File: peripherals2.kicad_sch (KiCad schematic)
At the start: 10 parts, among them J4 MSD-4-A, U8 GSDA213, U9 VEML3235SL

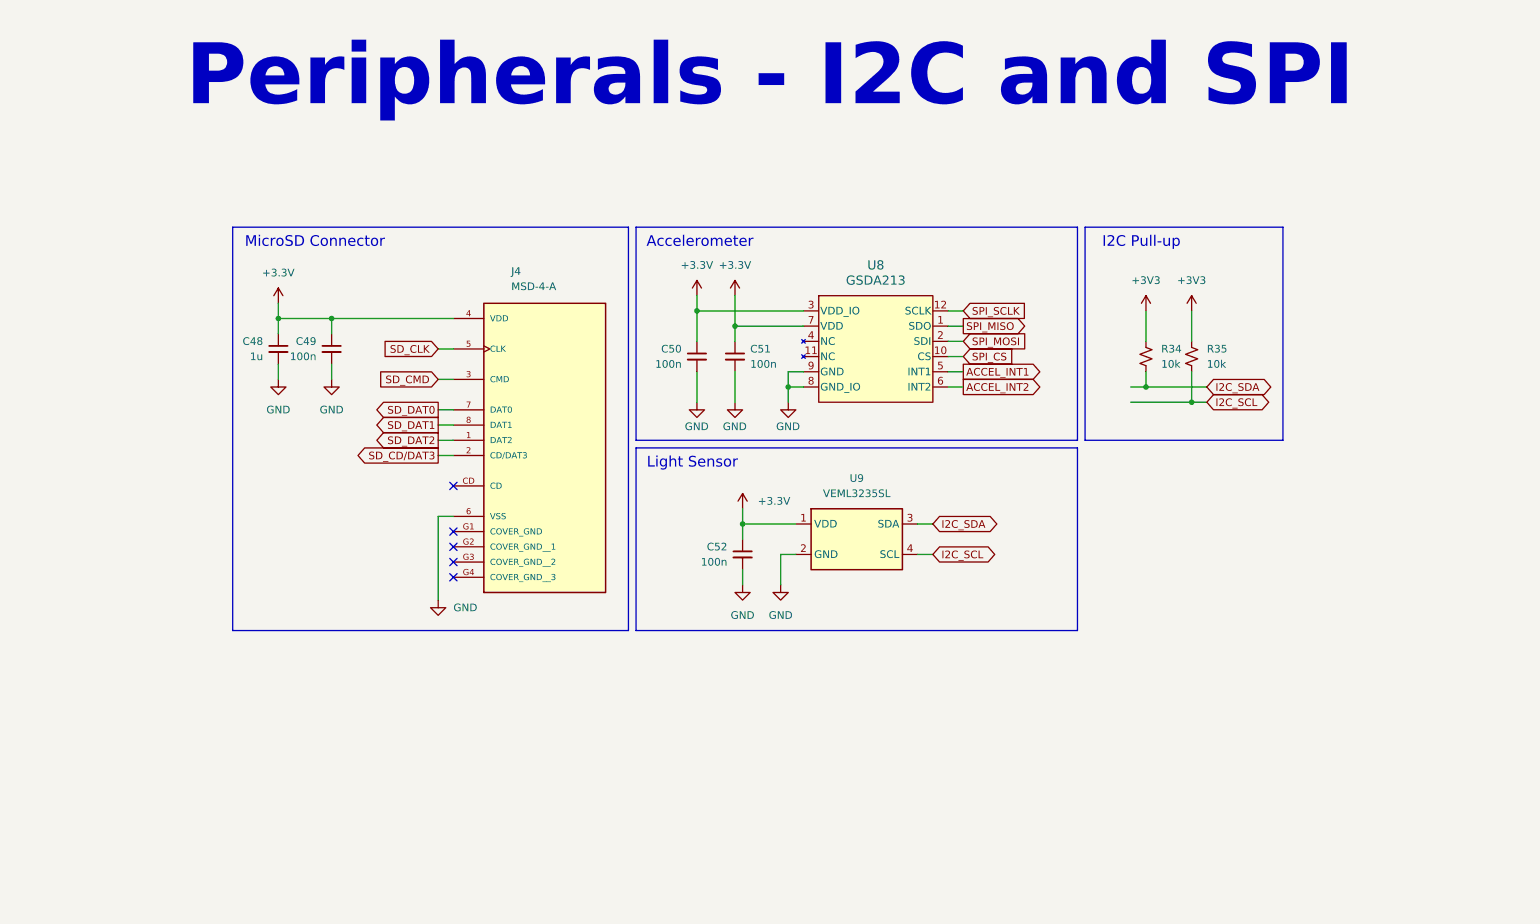
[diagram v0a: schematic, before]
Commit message: feat: adds display circuit
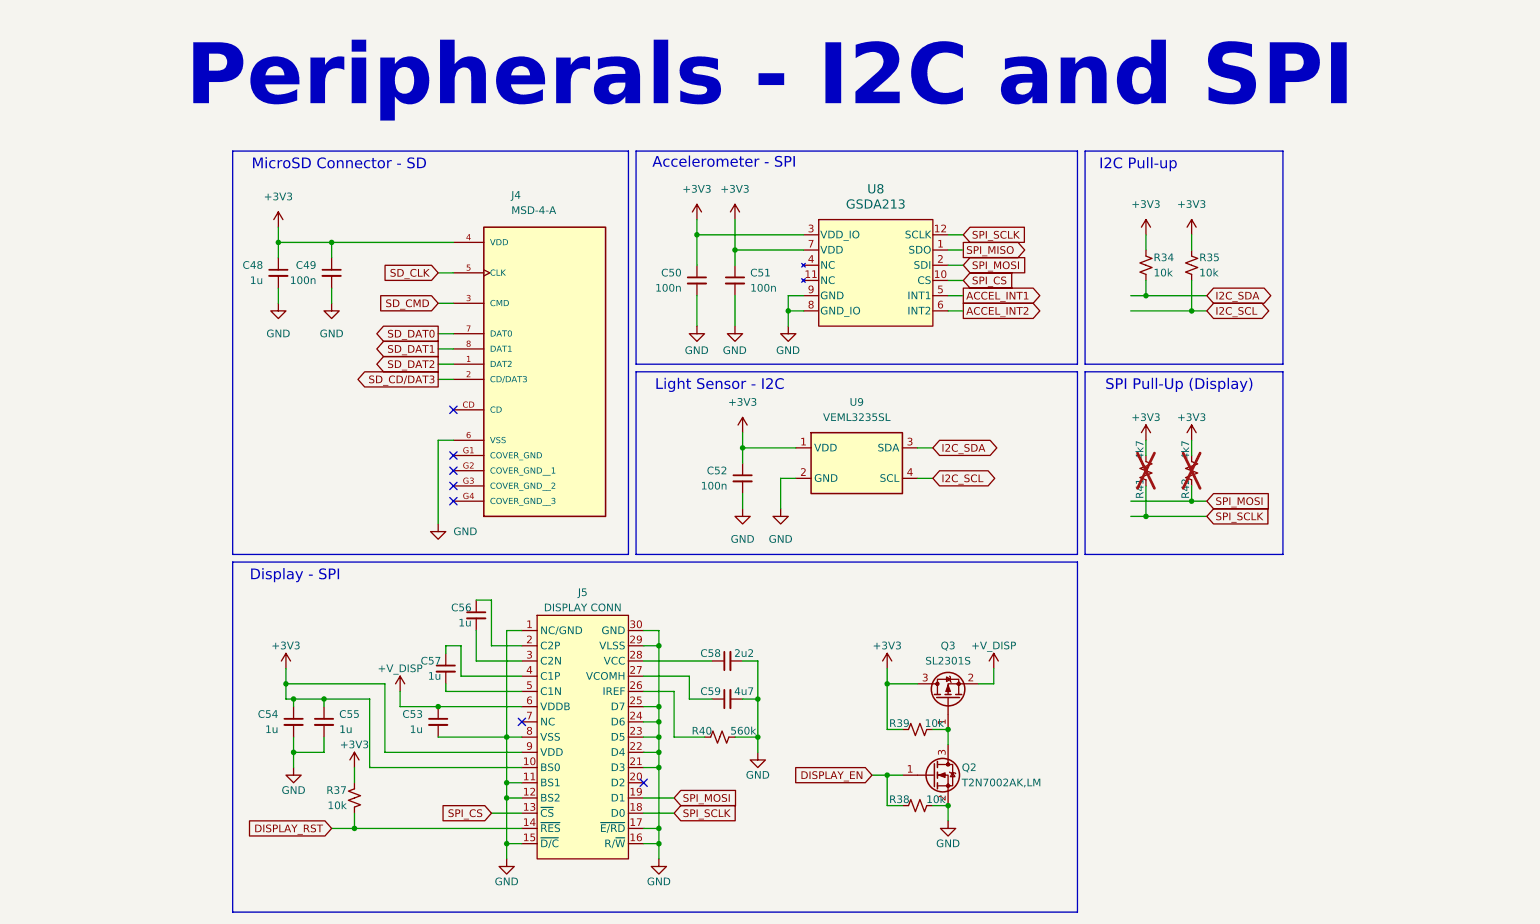
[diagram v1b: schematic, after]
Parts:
- added C53, C54, C55, C56, C57: 1u, Capacitor_SMD:C_0402_1005Metric, symbol Device:C_Small
- added C58: 2u2, Capacitor_SMD:C_0603_1608Metric, symbol Device:C_Small
- added C59: 4u7, Capacitor_SMD:C_0402_1005Metric, symbol Device:C_Small
- added J5: DISPLAY CONN, peripherals2:FPC_30, symbol peripherals2:DISPLAY_CONN
- added Q2: T2N7002AK,LM, Package_TO_SOT_SMD:SOT-23, symbol Transistor_FET:T2N7002AK
- added Q3: SL2301S, Package_TO_SOT_SMD:SOT-23, symbol Transistor_FET:AO3401A
- added R37, R38, R39: 10k, Resistor_SMD:R_0402_1005Metric, symbol Device:R_Small_US
- added R40: 560k, Resistor_SMD:R_0402_1005Metric, symbol Device:R_Small_US
- added R41, R42: 4k7, Resistor_SMD:R_0402_1005Metric, symbol Device:R_Small_US
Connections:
- net +3.3V is gone; now on net +3V3: C48.1, C49.1, C50.1, C51.1, C52.1, J4.4 (VDD), U8.3 (VDD_IO), U8.7 (VDD), U9.1 (VDD)
- net +3V3: now also C54.1, C55.1, J5.10 (BS0), J5.9 (VDD), Q3.3 (D), R37.1, R39.1, R41.2, R42.2
- net GND: now also C53.2, C54.2, C55.2, C58.2, C59.2, J5.1 (NC/GND), J5.11 (BS1), J5.12 (BS2), J5.15 (~{D/C}), J5.16 (R/~{W}), J5.17 (~{E/RD}), J5.21 (D3), J5.22 (D4), J5.23 (D5), J5.24 (D6), J5.25 (D7), J5.29 (VLSS), J5.30 (GND), J5.8 (VSS), Q2.2 (S), R38.2, R40.2
- net SPI_CS: now also J5.13 (~{CS})
- net SPI_MOSI: now also J5.19 (D1), R42.1
- net SPI_SCLK: now also J5.18 (D0), R41.1
- new net: C57.1, J5.4 (C1P)
- new net: C57.2, J5.5 (C1N)
- new net: C58.1, J5.28 (VCC)
- new net: Q2.3 (D), Q3.1 (G), R39.2
- new net: C56.1, J5.2 (C2P)
- new net: C56.2, J5.3 (C2N)
- new net: C59.1, J5.27 (VCOMH)
- new net: J5.26 (IREF), R40.1
- new net +V_DISP: C53.1, J5.6 (VDDB), Q3.2 (S)
- new net DISPLAY_EN: Q2.1 (G), R38.1
- new net DISPLAY_RST: J5.14 (~{RES}), R37.2
- no-connect marks 5 -> 7
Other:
- note added: "Accelerometer - SPI"
- note added: "Display - SPI"
- note added: "Light Sensor - I2C"
- note added: "MicroSD Connector - SD"
- note added: "SPI Pull-Up (Display)"
- note removed: "Accelerometer"
- note removed: "Light Sensor"
- note removed: "MicroSD Connector"
- moved on the sheet: C48, C49, C50, C51, C52, J4, R34, R35, U8, U9

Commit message: feat: connects SPI and I2C pins to MCU
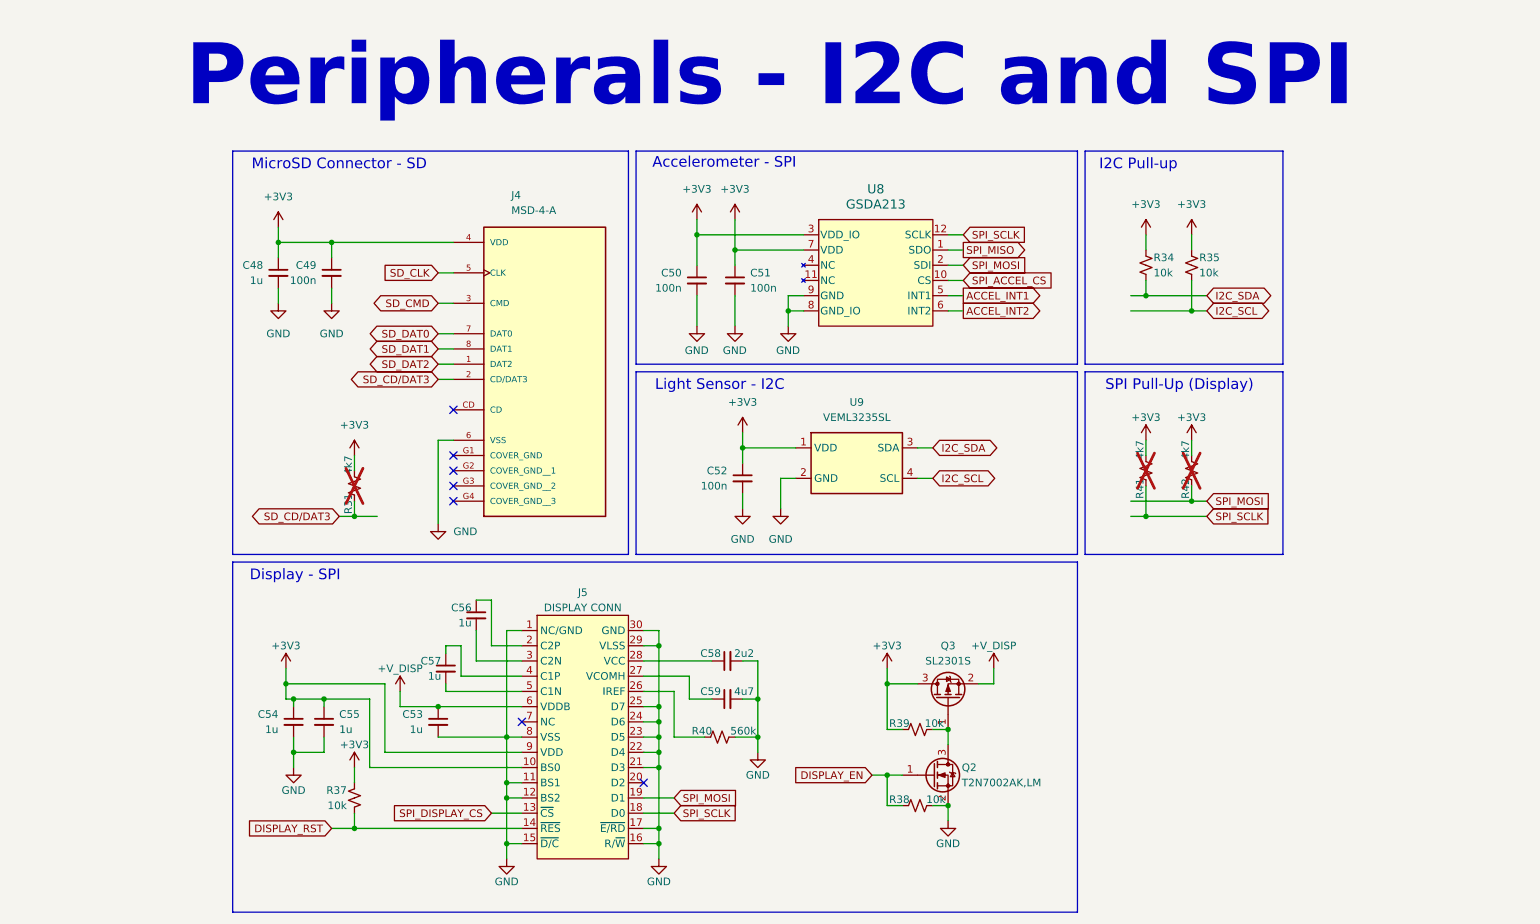
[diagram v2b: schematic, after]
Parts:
- added R31: 4k7, Resistor_SMD:R_0402_1005Metric, symbol Device:R_Small_US
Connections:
- net +3V3: now also R31.2
- net SD_CD/DAT3: now also R31.1
- net SPI_CS renamed SPI_ACCEL_CS
- net SPI_ACCEL_CS: no longer J5.13 (~{CS})
- new net SPI_DISPLAY_CS: J5.13 (~{CS})
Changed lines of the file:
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@@
 	)
 	(junction
+		(at 82.55 97.79)
+		(diameter 0)
+		(color 0 0 0 0)
+	)
+	(junction
 		(at 78.74 52.07)
 		(diameter 0)
@@
 	(wire
 		(pts
+			(xy 82.55 87.63) (xy 82.55 90.17)
+		)
+		(stroke
+			(width 0)
+			(type default)
+		)
+	)
+	(wire
+		(pts
+			(xy 82.55 97.79) (xy 86.36 97.79)
+		)
+		(stroke
+			(width 0)
+			(type default)
+		)
+	)
+	(wire
+		(pts
 			(xy 78.74 54.61) (xy 78.74 52.07)
 		)
@@
 	(wire
 		(pts
+			(xy 82.55 95.25) (xy 82.55 97.79)
+		)
+		(stroke
+			(width 0)
+			(type default)
+		)
+	)
+	(wire
+		(pts
 			(xy 72.39 137.16) (xy 72.39 139.7)
 		)
@@
 	(wire
 		(pts
+			(xy 82.55 97.79) (xy 80.01 97.79)
+		)
+		(stroke
+			(width 0)
+			(type default)
+		)
+	)
+	(wire
+		(pts
 			(xy 96.52 85.09) (xy 96.52 99.06)
 		)
@@
 	)
 	(global_label "SD_CD{slash}DAT3"
-		(shape output)
+		(shape bidirectional)
 		(at 96.52 74.93 180)
 		(fields_autoplaced yes)
@@
 		)
 	)
-	(global_label "SPI_CS"
+	(global_label "SPI_DISPLAY_CS"
 		(shape input)
 		(at 105.41 147.32 180)
@@
 		)
 		(property "Intersheetrefs" "${INTERSHEET_REFS}"
-			(at 95.8934 147.32 0)
+			(at 87.3662 147.32 0)
 			(effects
 				(font
@@
 		)
 	)
-	(global_label "SPI_CS"
+	(global_label "SPI_ACCEL_CS"
 		(shape input)
 		(at 184.15 58.42 0)
@@
 		)
 		(property "Intersheetrefs" "${INTERSHEET_REFS}"
-			(at 192.5553 58.42 0)
+			(at 200.4399 58.42 0)
 			(effects
 				(font
@@
 	)
 	(global_label "SD_DAT0"
-		(shape output)
+		(shape bidirectional)
 		(at 96.52 67.31 180)
 		(fields_autoplaced yes)
@@
 	)
 	(global_label "SD_CMD"
-		(shape input)
+		(shape bidirectional)
 		(at 96.52 62.23 180)
 		(fields_autoplaced yes)
@@
 	)
 	(global_label "SD_DAT1"
-		(shape output)
+		(shape bidirectional)
 		(at 96.52 69.85 180)
 		(fields_autoplaced yes)
@@
 	)
 	(global_label "SD_DAT2"
-		(shape output)
+		(shape bidirectional)
 		(at 96.52 72.39 180)
 		(fields_autoplaced yes)
@@
 		)
 	)
+	(global_label "SD_CD{slash}DAT3"
+		(shape bidirectional)
+		(at 80.01 97.79 180)
+		(fields_autoplaced yes)
+		(effects
+			(font
+				(size 1.27 1.27)
+			)
+			(justify right)
+		)
+		(property "Intersheetrefs" "${INTERSHEET_REFS}"
+			(at 66.2828 97.79 0)
+			(effects
+				(font
+					(size 1.27 1.27)
+				)
+				(justify right)
+				(hide yes)
+			)
+		)
+	)
 	(global_label "DISPLAY_RST"
 		(shape input)
@@
 	)
 	(symbol
+		(lib_id "Device:R_Small_US")
+		(at 82.55 92.71 180)
+		(unit 1)
+		(exclude_from_sim no)
+		(in_bom yes)
+		(on_board yes)
+		(dnp yes)
+		(property "Reference" "R31"
+			(at 81.534 93.98 90)
+			(effects
+				(font
+					(size 1.27 1.27)
+				)
+				(justify left)
+			)
+		)
+		(property "Value" "4k7"
+			(at 81.534 87.63 90)
+			(effects
+				(font
+					(size 1.27 1.27)
+				)
+				(justify left)
+			)
+		)
+		(property "Footprint" "Resistor_SMD:R_0402_1005Metric"
+			(at 82.55 92.71 0)
+			(effects
+				(font
+					(size 1.27 1.27)
+				)
+				(hide yes)
+			)
+		)
+		(property "Datasheet" "https://www.digikey.com.br/en/products/detail/yageo/RC0402JR-074K7L/726477"
+			(at 82.55 92.71 0)
+			(effects
+				(font
+					(size 1.27 1.27)
+				)
+				(hide yes)
+			)
+		)
+		(property "Description" "Resistor, small US symbol"
+			(at 82.55 92.71 0)
+			(effects
+				(font
+					(size 1.27 1.27)
+				)
+				(hide yes)
+			)
+		)
+		(property "MPN" "RC0402JR-074K7L"
+			(at 82.55 92.71 0)
+			(effects
+				(font
+					(size 1.27 1.27)
+				)
+				(hide yes)
+			)
+		)
+		(pin "2"
+		)
+		(pin "1"
+		)
+		(instances
+			(project "zbook"
+				(path "/b90666d0-8852-4bb1-832d-f9d855027372/e26c05ee-f364-47de-be04-e77902e037c8"
+					(reference "R31")
+					(unit 1)
+				)
+			)
+		)
+	)
+	(symbol
 		(lib_id "peripherals2:DISPLAY_CONN")
 		(at 120.65 133.35 0)
@@
 					(unit 1)
 				)
+			)
+		)
+	)
+	(symbol
+		(lib_id "power:+3V3")
+		(at 82.55 87.63 0)
+		(unit 1)
+		(exclude_from_sim no)
+		(in_bom yes)
+		(on_board yes)
+		(dnp no)
+		(fields_autoplaced yes)
+		(property "Reference" "#PWR0119"
+			(at 82.55 91.44 0)
+			(effects
+				(font
+					(size 1.27 1.27)
+				)
+				(hide yes)
+			)
+		)
+		(property "Value" "+3V3"
+			(at 82.55 82.55 0)
+			(effects
+				(font
+					(size 1.27 1.27)
+				)
+			)
+		)
+		(property "Footprint" ""
+			(at 82.55 87.63 0)
+			(effects
+				(font
+					(size 1.27 1.27)
+				)
+				(hide yes)
+			)
+		)
+		(property "Datasheet" ""
+			(at 82.55 87.63 0)
+			(effects
+				(font
+					(size 1.27 1.27)
+				)
+				(hide yes)
+			)
+		)
+		(property "Description" "Power symbol creates a global label with name \"+3V3\""
+			(at 82.55 87.63 0)
+			(effects
+				(font
+					(size 1.27 1.27)
+				)
+				(hide yes)
+			)
+		)
+		(pin "1"
+		)
+		(instances
+			(project "zbook"
+				(path "/b90666d0-8852-4bb1-832d-f9d855027372/e26c05ee-f364-47de-be04-e77902e037c8"
+					(reference "#PWR0119")
+					(unit 1)
+				)
